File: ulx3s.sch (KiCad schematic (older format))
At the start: 9 parts, among them J2 JACK_TRS_6PINS, P1 USB_FTDI, P2 USB_FPGA, U1 LFE5-BG381, U2 ESP-12E

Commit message: Departing from RPI-0 size to a 56x106 mm board
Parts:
- P1, P2: symbol USB_OTG -> USB_OTG-RESCUE-ulx3s
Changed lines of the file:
@@
 EESchema Schematic File Version 2
+LIBS:ulx3s-rescue
 LIBS:power
 LIBS:device
@@
 $EndDescr
 $Comp
-L GND #PWR1
+L GND #PWR01
 U 1 1 56ABA99F
 P 1100 2650
-F 0 "#PWR1" H 1100 2400 50  0001 C CNN
+F 0 "#PWR01" H 1100 2400 50  0001 C CNN
 F 1 "GND" H 1100 2500 50  0000 C CNN
 F 2 "" H 1100 2650 60  0000 C CNN
@@
 $EndComp
 $Comp
-L VCC #PWR2
+L VCC #PWR02
 U 1 1 56ABAA88
 P 2250 950
-F 0 "#PWR2" H 2250 800 50  0001 C CNN
+F 0 "#PWR02" H 2250 800 50  0001 C CNN
 F 1 "VCC" H 2250 1100 50  0000 C CNN
 F 2 "" H 2250 950 60  0000 C CNN
@@
 	4600 4950 4700 4950
 $Comp
-L GND #PWR3
+L GND #PWR03
 U 1 1 56ACA1D2
 P 4700 4950
-F 0 "#PWR3" H 4700 4700 50  0001 C CNN
+F 0 "#PWR03" H 4700 4700 50  0001 C CNN
 F 1 "GND" H 4700 4800 50  0000 C CNN
 F 2 "" H 4700 4950 60  0000 C CNN
@@
 $EndComp
 $Comp
-L USB_OTG P1
+L USB_OTG-RESCUE-ulx3s P1
 U 1 1 56ACC213
 P 5200 6350
@@
 $EndComp
 $Comp
-L USB_OTG P2
+L USB_OTG-RESCUE-ulx3s P2
 U 1 1 56ACC38E
 P 5200 7300
@@
 	6050 6150 6200 6150
 $Comp
-L +5V #PWR5
+L +5V #PWR04
 U 1 1 56AA16D2
 P 6200 6150
-F 0 "#PWR5" H 6200 6000 50  0001 C CNN
+F 0 "#PWR04" H 6200 6000 50  0001 C CNN
 F 1 "+5V" H 6200 6290 50  0000 C CNN
 F 2 "" H 6200 6150 60  0000 C CNN
@@
 	5500 7100 5600 7100
 $Comp
-L +5V #PWR4
+L +5V #PWR05
 U 1 1 56AA305B
 P 5950 7100
-F 0 "#PWR4" H 5950 6950 50  0001 C CNN
+F 0 "#PWR05" H 5950 6950 50  0001 C CNN
 F 1 "+5V" H 5950 7240 50  0000 C CNN
 F 2 "" H 5950 7100 60  0000 C CNN

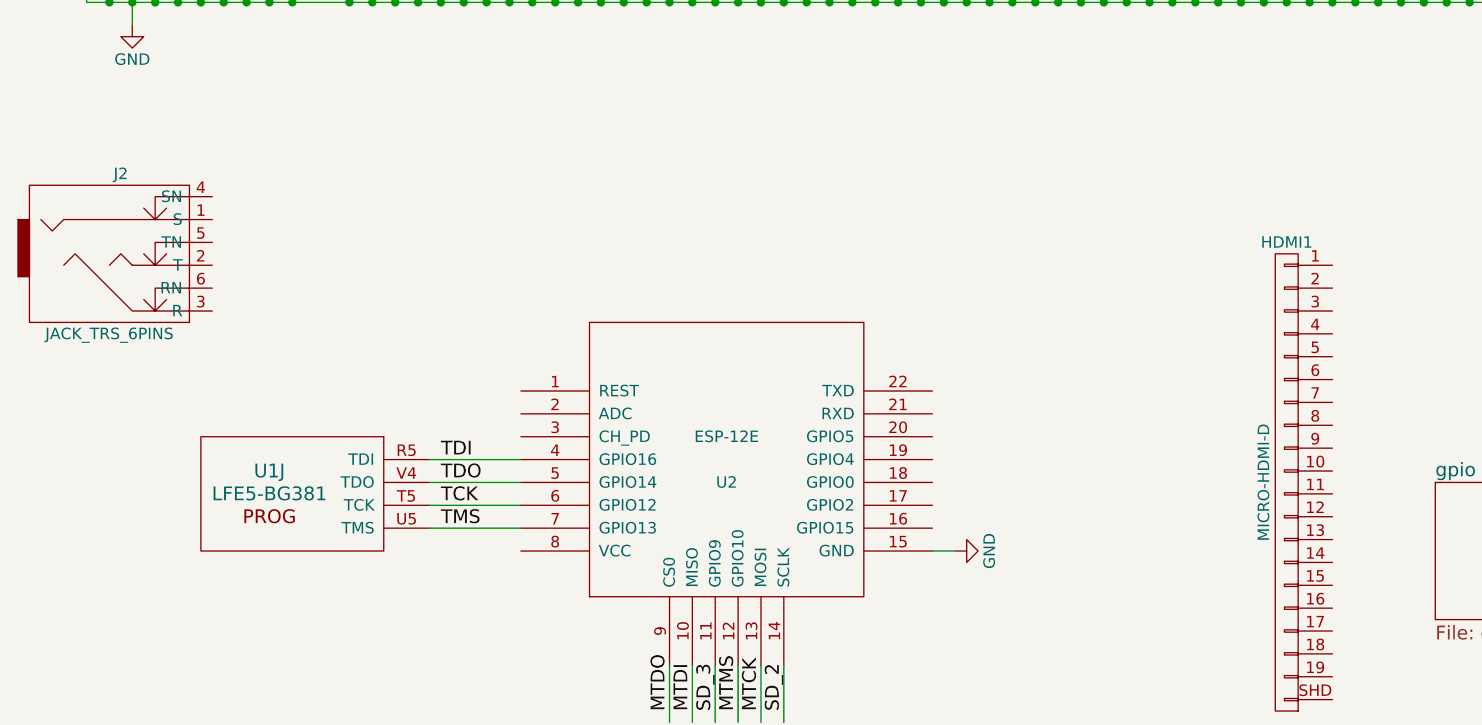
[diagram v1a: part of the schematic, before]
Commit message: using connectors 2x32 for general purpose and 2x15 for 2 PMODs Board is now a bit smaller
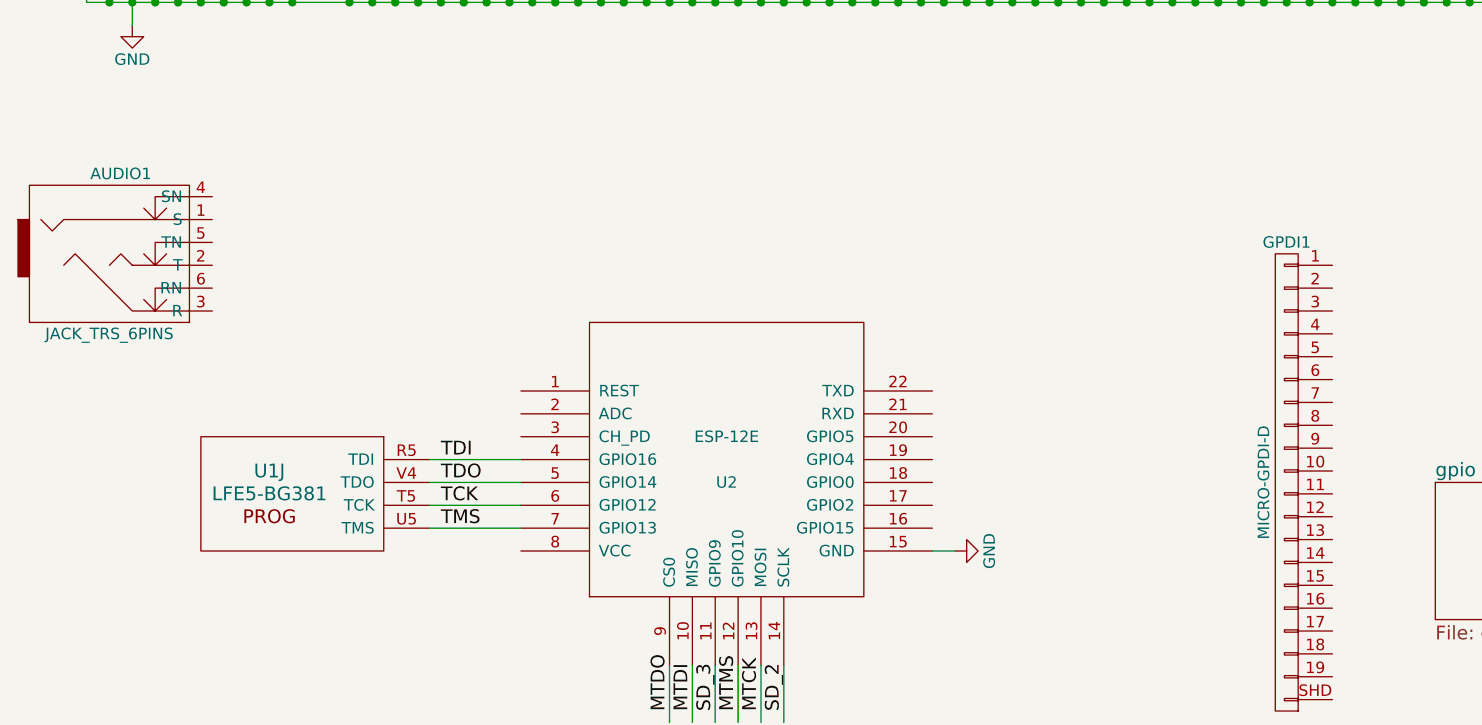
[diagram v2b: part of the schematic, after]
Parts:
- GPDI1: renamed from HDMI1; value MICRO-HDMI-D -> MICRO-GPDI-D
- renumbered J2 to AUDIO1
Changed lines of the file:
@@
 EESchema Schematic File Version 2
-LIBS:ulx3s-rescue
 LIBS:power
 LIBS:device
@@
 $EndComp
 $Comp
-L MICRO-HDMI-D HDMI1
+L MICRO-HDMI-D GPDI1
 U 1 1 56ACD5D4
 P 6150 4650
-F 0 "HDMI1" H 6150 5700 50  0000 C CNN
-F 1 "MICRO-HDMI-D" V 6250 4650 50  0000 C CNN
+F 0 "GPDI1" H 6150 5700 50  0000 C CNN
+F 1 "MICRO-GPDI-D" V 6250 4650 50  0000 C CNN
 F 2 "micro-hdmi-d:MICRO-HDMI-D" H 6150 4650 60  0001 C CNN
 F 3 "" H 6150 4650 60  0000 C CNN
@@
 $EndComp
 $Comp
-L JACK_TRS_6PINS J2
+L JACK_TRS_6PINS AUDIO1
 U 1 1 56A9D95B
 P 1050 3700
-F 0 "J2" H 1050 4100 50  0000 C CNN
+F 0 "AUDIO1" H 1050 4100 50  0000 C CNN
 F 1 "JACK_TRS_6PINS" H 1000 3400 50  0000 C CNN
 F 2 "" H 1150 3550 60  0001 C CNN

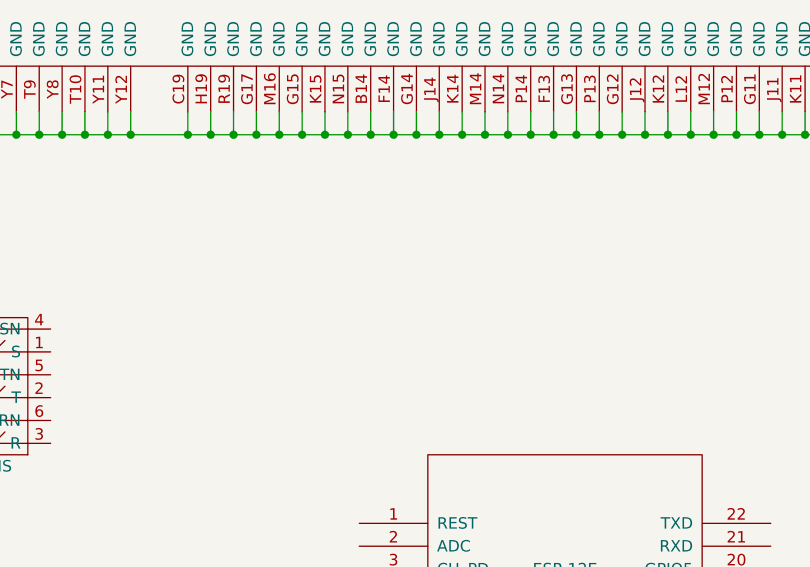
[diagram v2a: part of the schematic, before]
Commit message: Reduce board size to 92.5 x 49.3 mm, reshuffle components.
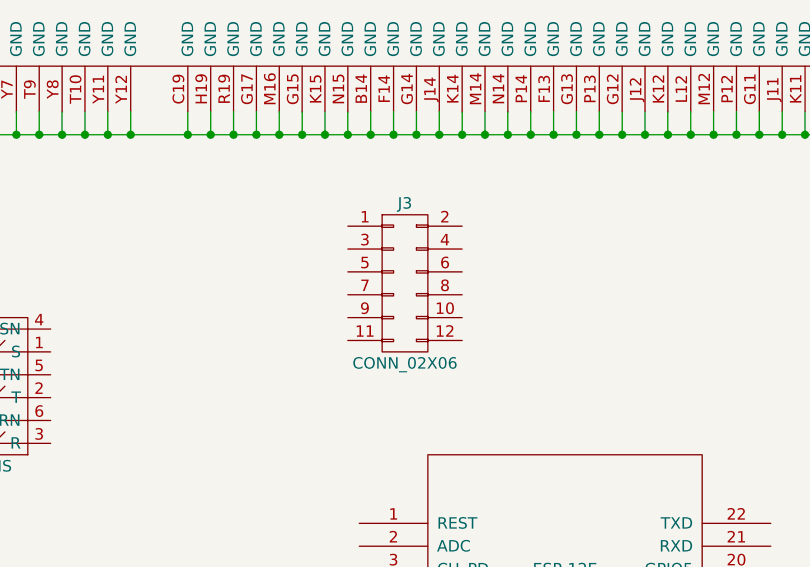
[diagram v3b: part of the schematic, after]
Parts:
- added J3: CONN_02X06, Socket_Strips:Socket_Strip_Angled_2x06_Pitch2.54mm, symbol CONN_02X06
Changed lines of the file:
@@
 F1 "gpio.sch" 60
 $EndSheet
+$Comp
+L CONN_02X06 J3
+U 1 1 58D3C869
+P 3000 3200
+F 0 "J3" H 3000 3550 50  0000 C CNN
+F 1 "CONN_02X06" H 3000 2850 50  0000 C CNN
+F 2 "Socket_Strips:Socket_Strip_Angled_2x06_Pitch2.54mm" H 3000 2000 50  0001 C CNN
+F 3 "" H 3000 2000 50  0001 C CNN
+	1    3000 3200
+	1    0    0    -1
+$EndComp
 $EndSCHEMATC

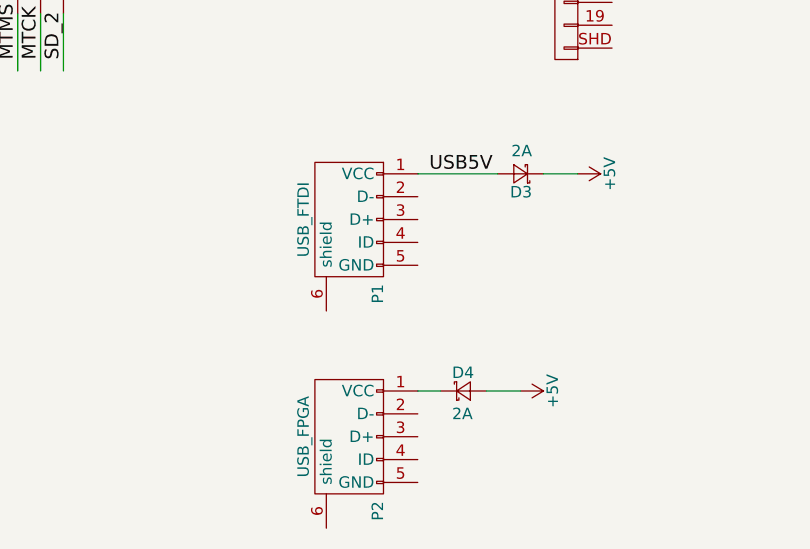
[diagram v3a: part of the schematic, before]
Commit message: add missing library footprint/usb_otg
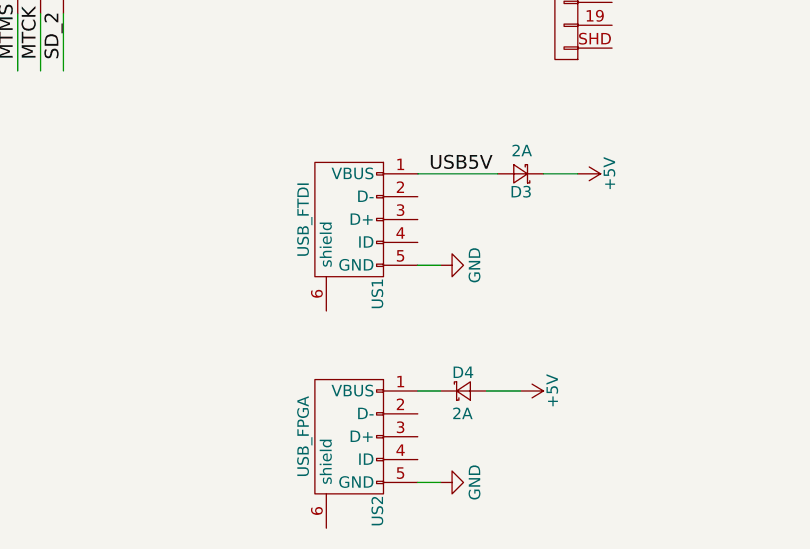
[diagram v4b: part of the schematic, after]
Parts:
- removed P1: USB_FTDI, Connect:USB_Micro-B, symbol USB_OTG-RESCUE-ulx3s
- removed P2: USB_FPGA, Connect:USB_Micro-B, symbol USB_OTG-RESCUE-ulx3s
- added US1: USB_FTDI, usb_otg:USB_Micro-B, symbol USB_OTG
- added US2: USB_FPGA, usb_otg:USB_Micro-B, symbol USB_OTG
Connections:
- wire segments 164 -> 166
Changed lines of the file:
@@
 EESchema Schematic File Version 2
+LIBS:ulx3s-rescue
 LIBS:power
 LIBS:device
@@
 $EndComp
 $Comp
-L USB_OTG-RESCUE-ulx3s P1
-U 1 1 56ACC213
-P 5200 6350
-F 0 "P1" H 5525 6225 50  0000 C CNN
-F 1 "USB_FTDI" H 5200 6550 50  0000 C CNN
-F 2 "Connect:USB_Micro-B" V 5150 6250 60  0001 C CNN
-F 3 "" V 5150 6250 60  0000 C CNN
-	1    5200 6350
-	0    -1   1    0
-$EndComp
-$Comp
-L USB_OTG-RESCUE-ulx3s P2
-U 1 1 56ACC38E
-P 5200 7300
-F 0 "P2" H 5525 7175 50  0000 C CNN
-F 1 "USB_FPGA" H 5200 7500 50  0000 C CNN
-F 2 "Connect:USB_Micro-B" V 5150 7200 60  0001 C CNN
-F 3 "" V 5150 7200 60  0000 C CNN
-	1    5200 7300
-	0    -1   1    0
-$EndComp
-$Comp
 L MICRO-HDMI-D GPDI1
 U 1 1 56ACD5D4
@@
 	1    0    0    -1
 $EndComp
+$Comp
+L USB_OTG US1
+U 1 1 58D432CE
+P 5200 6350
+F 0 "US1" H 5525 6225 50  0000 C CNN
+F 1 "USB_FTDI" H 5200 6550 50  0000 C CNN
+F 2 "usb_otg:USB_Micro-B" V 5150 6250 50  0001 C CNN
+F 3 "" V 5150 6250 50  0000 C CNN
+	1    5200 6350
+	0    -1   1    0
+$EndComp
+$Comp
+L USB_OTG US2
+U 1 1 58D4378B
+P 5200 7300
+F 0 "US2" H 5525 7175 50  0000 C CNN
+F 1 "USB_FPGA" H 5200 7500 50  0000 C CNN
+F 2 "usb_otg:USB_Micro-B" V 5150 7200 50  0001 C CNN
+F 3 "" V 5150 7200 50  0000 C CNN
+	1    5200 7300
+	0    -1   1    0
+$EndComp
+$Comp
+L GND #PWR06
+U 1 1 58D43846
+P 5600 6550
+F 0 "#PWR06" H 5600 6300 50  0001 C CNN
+F 1 "GND" H 5600 6400 50  0000 C CNN
+F 2 "" H 5600 6550 50  0000 C CNN
+F 3 "" H 5600 6550 50  0000 C CNN
+	1    5600 6550
+	0    -1   -1   0
+$EndComp
+Wire Wire Line
+	5500 6550 5600 6550
+Wire Wire Line
+	5500 7500 5600 7500
+$Comp
+L GND #PWR07
+U 1 1 58D43AF2
+P 5600 7500
+F 0 "#PWR07" H 5600 7250 50  0001 C CNN
+F 1 "GND" H 5600 7350 50  0000 C CNN
+F 2 "" H 5600 7500 50  0000 C CNN
+F 3 "" H 5600 7500 50  0000 C CNN
+	1    5600 7500
+	0    -1   -1   0
+$EndComp
 $EndSCHEMATC

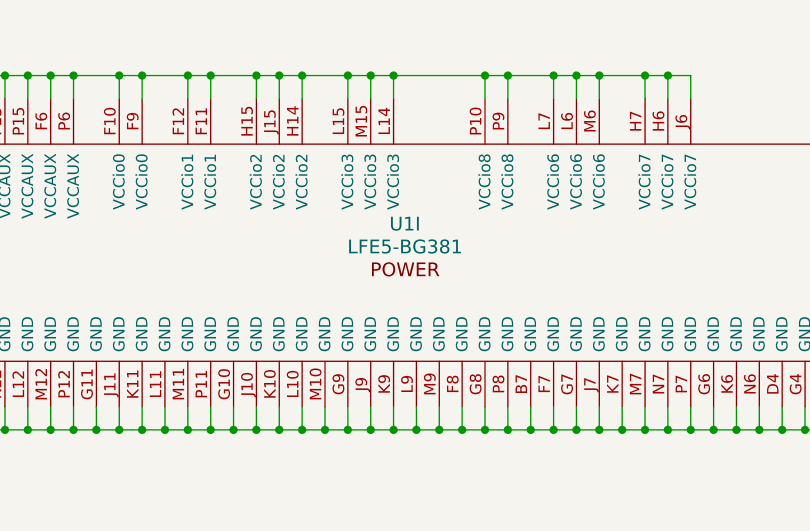
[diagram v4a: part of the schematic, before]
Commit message: changing chip name and slightly reordering blocks in the schematics
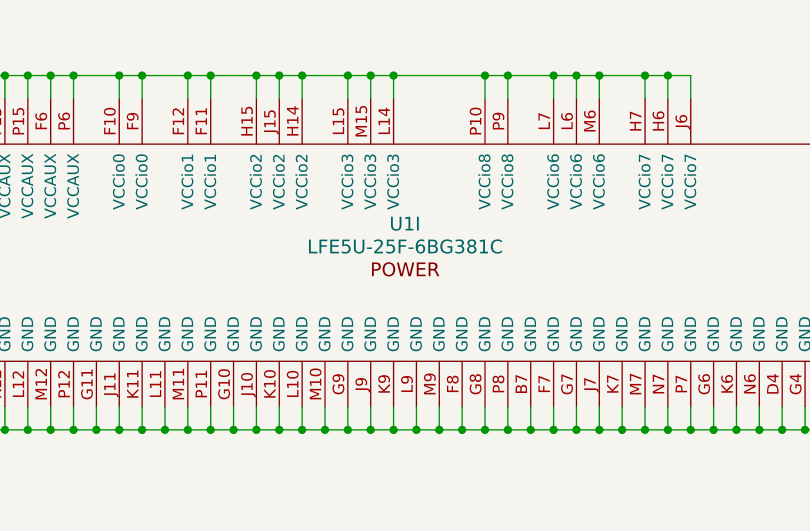
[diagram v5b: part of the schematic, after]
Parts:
- U1: value LFE5-BG381 -> LFE5U-25F-6BG381C
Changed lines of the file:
@@
 P 5900 1750
 F 0 "U1" H 5900 1850 60  0000 C CNN
-F 1 "LFE5-BG381" H 5900 1750 60  0000 C CNN
+F 1 "LFE5U-25F-6BG381C" H 5900 1750 60  0000 C CNN
 F 2 "lfe5bg381:BGA-381_pitch0.8mm_dia0.4mm" H 4850 2700 60  0001 C CNN
 F 3 "" H 4850 2700 60  0000 C CNN

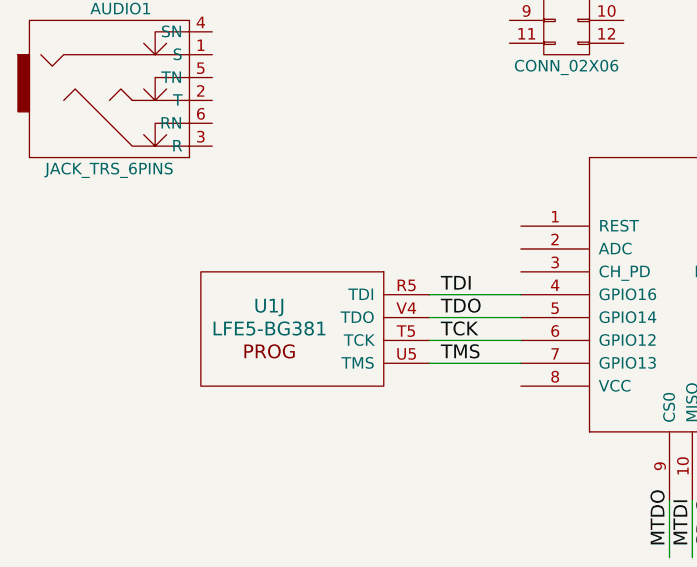
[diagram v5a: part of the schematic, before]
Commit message: chip name edited on JTAG to be the same as all units
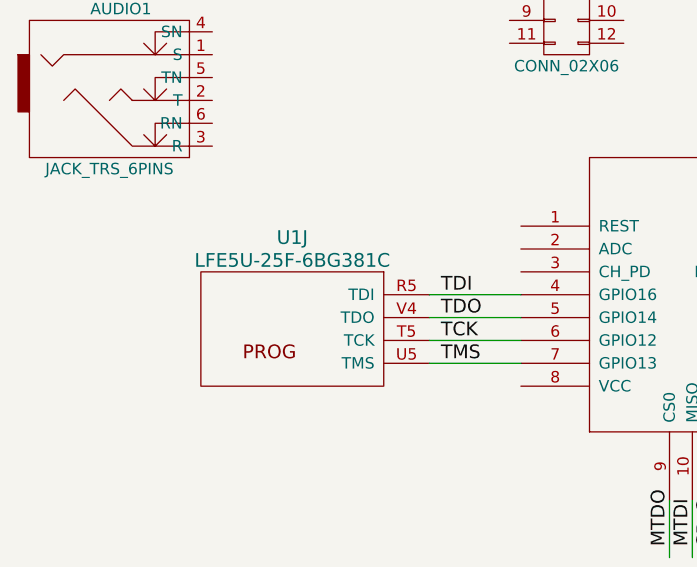
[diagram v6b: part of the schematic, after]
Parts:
- U1: value LFE5-BG381 -> LFE5U-25F-6BG381C
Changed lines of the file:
@@
 U 10 1 56AAA6F3
 P 1700 4700
-F 0 "U1" H 1700 4800 60  0000 C CNN
-F 1 "LFE5-BG381" H 1700 4700 60  0000 C CNN
+F 0 "U1" H 1600 5100 60  0000 C CNN
+F 1 "LFE5U-25F-6BG381C" H 1600 5000 60  0000 C CNN
 F 2 "lfe5bg381:BGA-381_pitch0.8mm_dia0.4mm" H 650 5650 60  0001 C CNN
 F 3 "" H 650 5650 60  0000 C CNN

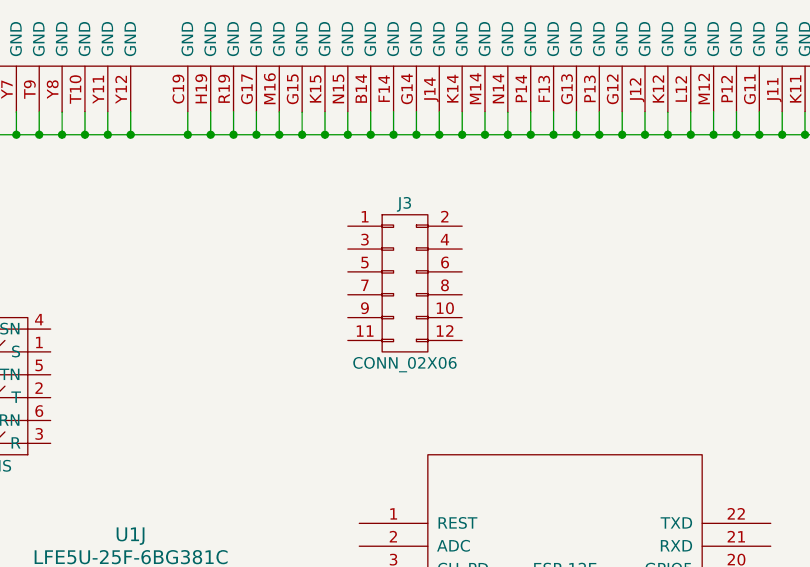
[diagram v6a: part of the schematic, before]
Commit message: shrinking the board
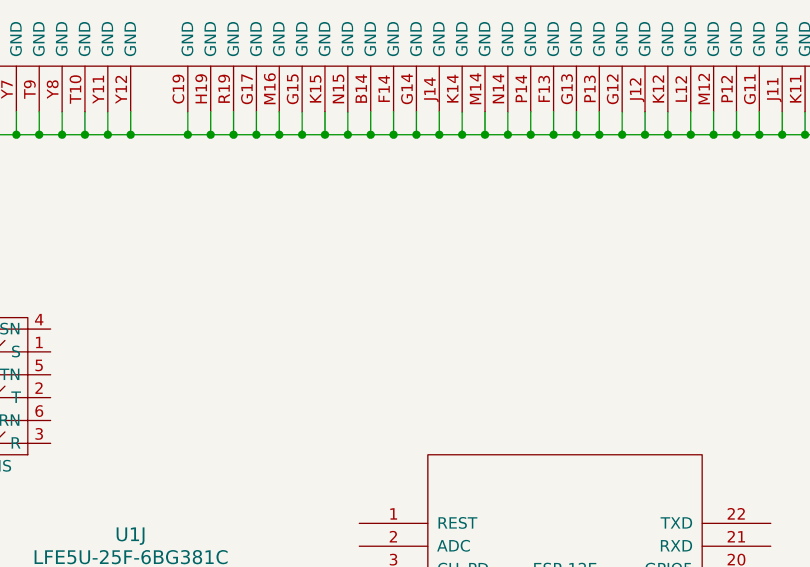
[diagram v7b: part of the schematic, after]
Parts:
- removed J3: CONN_02X06, Socket_Strips:Socket_Strip_Angled_2x06_Pitch2.54mm, symbol CONN_02X06
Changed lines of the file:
@@
 $EndSheet
-$Comp
-L CONN_02X06 J3
-U 1 1 58D3C869
-P 3000 3200
-F 0 "J3" H 3000 3550 50  0000 C CNN
-F 1 "CONN_02X06" H 3000 2850 50  0000 C CNN
-F 2 "Socket_Strips:Socket_Strip_Angled_2x06_Pitch2.54mm" H 3000 2000 50  0001 C CNN
-F 3 "" H 3000 2000 50  0001 C CNN
-	1    3000 3200
-	1    0    0    -1
-$EndComp
 $Comp
 L USB_OTG US1
